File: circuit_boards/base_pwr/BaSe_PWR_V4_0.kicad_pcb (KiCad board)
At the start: 4 copper layers, 114.2 x 101.5 mm, 101 parts, among them J1 12VDC In, J10 Conn_01x04_Socket, J11 MOTOR, J12 USB3_A, J3 USB_B_Micro, J4 Conn_01x07_Pin, J5 Conn_02x06_Odd_Even, J6 USB3_B_Micro, J7 Conn_02x06_Odd_Even, J8 USB_C_Receptacle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

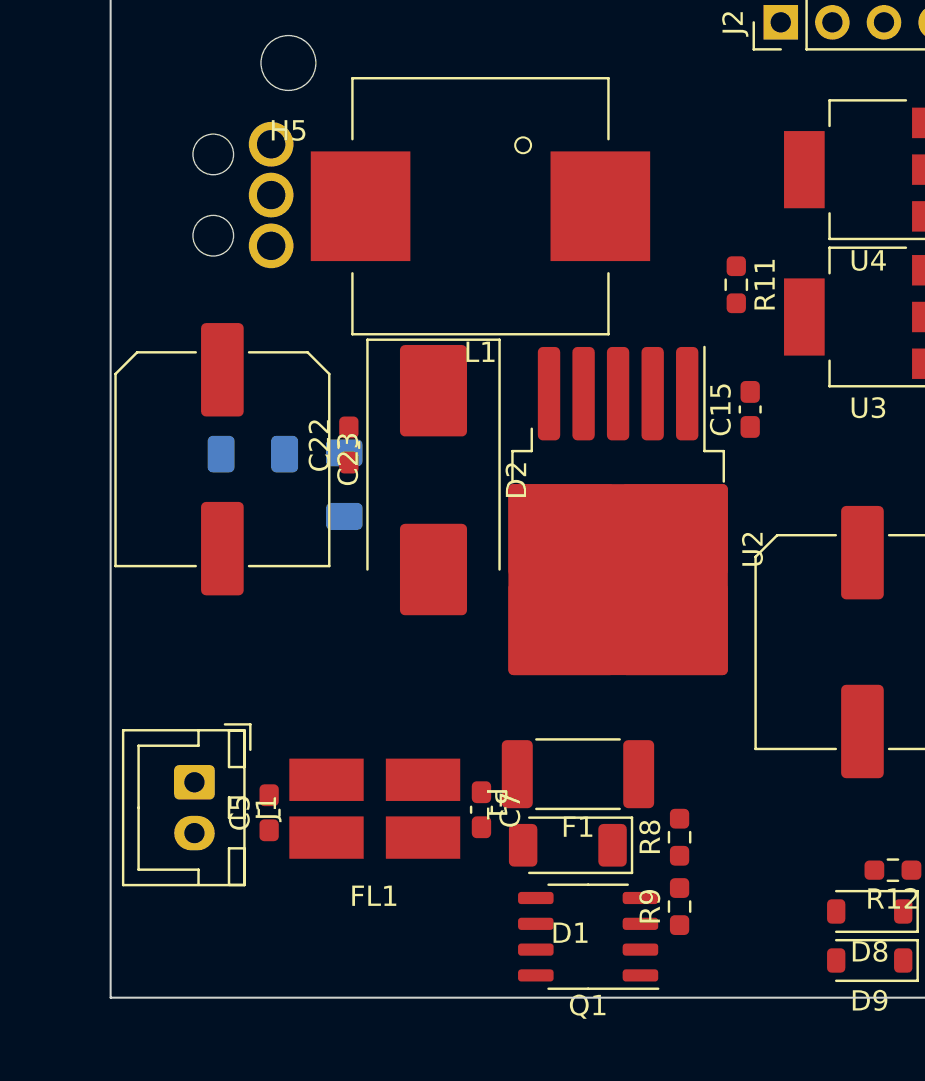
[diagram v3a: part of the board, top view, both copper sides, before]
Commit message: BaSe PWR V4.0: quasi final positioning before actual routing phase
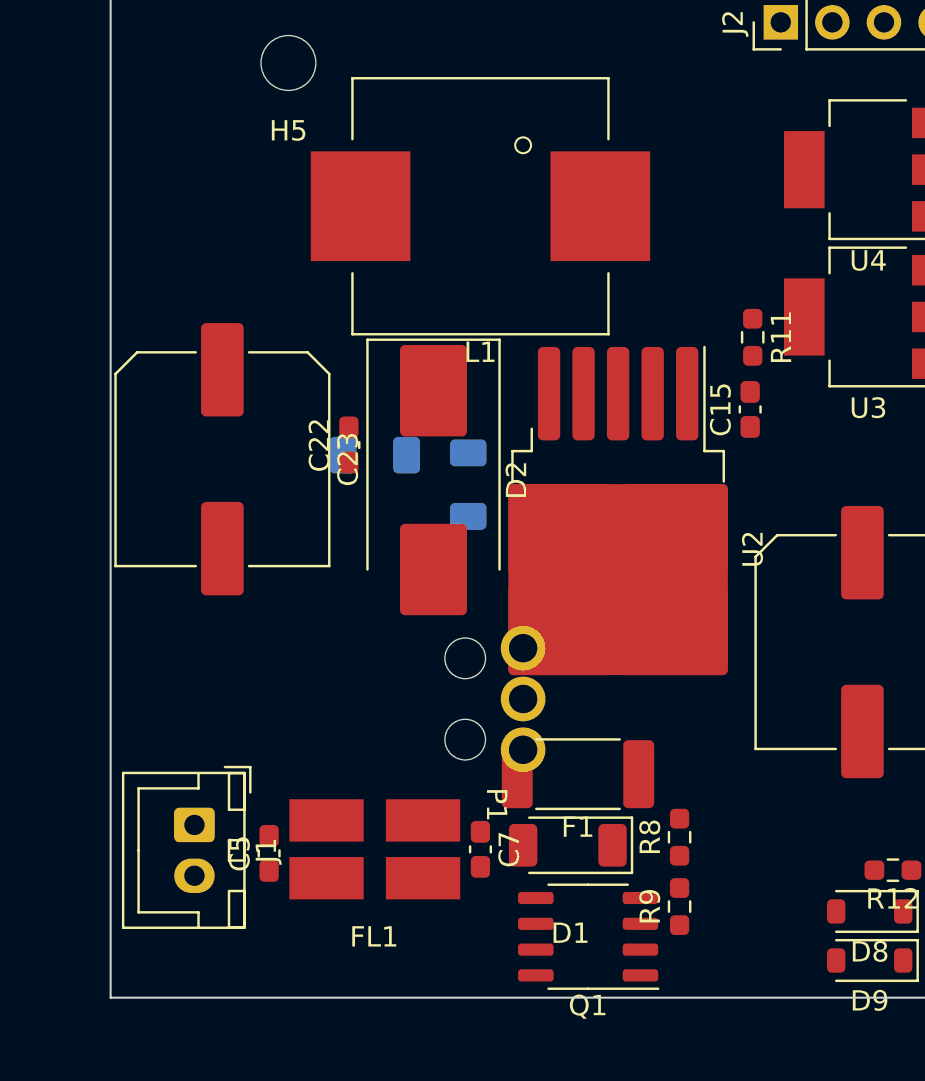
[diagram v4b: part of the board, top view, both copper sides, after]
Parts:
- moved U6 27.7 mm to (40.3, 98.8)
- moved C26 6.10 mm to (37.6, 88.2)
- moved FB1 6.00 mm to (33.0, 86.8)
- moved R11 2.71 mm to (51.6, 81.0)
- moved J1 2.10 mm to (24.1, 105.0)
- moved C5 2.00 mm to (27.8, 106.4)
- moved FL1 2.00 mm to (33.0, 106.2)
- moved C7 1.95 mm to (38.2, 106.2)
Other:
- board text added: "No Components here on BOTTOM"
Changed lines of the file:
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@@
   )
   (footprint "Capacitor_SMD:C_0603_1608Metric_Pad1.08x0.95mm_HandSolder" (layer "F.Cu")
-    (at 27.8 104.4 90)
+    (at 27.8 106.4 90)
     (descr "Capacitor SMD 0603 (1608 Metric), square (rectangular) end terminal, IPC_7351 nominal with elongated pad for handsoldering. (Body size source: IPC-SM-782 page 76, https://www.pcb-3d.com/wordpress/wp-content/uploads/ipc-sm-782a_amendment_1_and_2.pdf), generated with kicad-footprint-generator")
     (tags "capacitor handsolder")
@@
   )
   (footprint "Connector_JST:JST_XH_B2B-XH-A_1x02_P2.50mm_Vertical" (layer "F.Cu")
-    (at 24.125 102.9 -90)
+    (at 24.125 105 -90)
     (descr "JST XH series connector, B2B-XH-A (http://www.jst-mfg.com/product/pdf/eng/eXH.pdf), generated with kicad-footprint-generator")
     (tags "connector JST XH vertical")
@@
   )
   (footprint "Capacitor_SMD:C_0603_1608Metric_Pad1.08x0.95mm_HandSolder" (layer "F.Cu")
-    (at 38.25 104.25 -90)
+    (at 38.2 106.2 -90)
     (descr "Capacitor SMD 0603 (1608 Metric), square (rectangular) end terminal, IPC_7351 nominal with elongated pad for handsoldering. (Body size source: IPC-SM-782 page 76, https://www.pcb-3d.com/wordpress/wp-content/uploads/ipc-sm-782a_amendment_1_and_2.pdf), generated with kicad-footprint-generator")
     (tags "capacitor handsolder")
@@
   )
   (footprint "g7_emi:CMC_Laird_CM2021Y330R-10" (layer "F.Cu")
-    (at 33 104.2)
+    (at 33 106.2)
     (property "SPN" "240-2502-1-ND")
     (property "Sheetfile" "BaSe_PWR_V4_0.kicad_sch")
@@
   )
   (footprint "Resistor_SMD:R_0603_1608Metric_Pad0.98x0.95mm_HandSolder" (layer "F.Cu")
-    (at 50.79 78.4125 -90)
+    (at 51.6 81 -90)
     (descr "Resistor SMD 0603 (1608 Metric), square (rectangular) end terminal, IPC_7351 nominal with elongated pad for handsoldering. (Body size source: IPC-SM-782 page 72, https://www.pcb-3d.com/wordpress/wp-content/uploads/ipc-sm-782a_amendment_1_and_2.pdf), generated with kicad-footprint-generator")
     (tags "resistor handsolder")
@@
   )
   (footprint "Capacitor_SMD:C_1206_3216Metric_Pad1.33x1.80mm_HandSolder" (layer "B.Cu")
-    (at 31.5 88.25 90)
+    (at 37.6 88.25 90)
     (descr "Capacitor SMD 1206 (3216 Metric), square (rectangular) end terminal, IPC_7351 nominal with elongated pad for handsoldering. (Body size source: IPC-SM-782 page 76, https://www.pcb-3d.com/wordpress/wp-content/uploads/ipc-sm-782a_amendment_1_and_2.pdf), generated with kicad-footprint-generator")
     (tags "capacitor handsolder")
@@
     )
   )
-  (footprint "g7_switch:TS0101F020V4" (layer "B.Cu")
-    (at 27.9 74 -90)
+  (footprint "g7_switch:TS0101F020V4" locked (layer "B.Cu")
+    (at 40.3 98.8 -90)
     (property "Digikey" "EG4938-ND")
     (property "Sheetfile" "BaSe_PWR_V4_0.kicad_sch")
@@
     (fp_line (start 4.1 7.85) (end 4.1 1.25)
       (stroke (width 0.1) (type default)) (layer "B.Fab"))
-    (pad "" np_thru_hole circle (at -2 2.85 270) (size 2 2) (drill 2) (layers "F&B.Cu" "*.Mask"))
-    (pad "" np_thru_hole circle (at 2 2.85 270) (size 2 2) (drill 2) (layers "F&B.Cu" "*.Mask"))
-    (pad "C" thru_hole circle (at -2.5 0 270) (size 2.2 2.2) (drill 1.4) (layers "*.Cu" "*.Mask")
+    (pad "" np_thru_hole circle locked (at -2 2.85 270) (size 2 2) (drill 2) (layers "F&B.Cu" "*.Mask"))
+    (pad "" np_thru_hole circle locked (at 2 2.85 270) (size 2 2) (drill 2) (layers "F&B.Cu" "*.Mask"))
+    (pad "C" thru_hole circle locked (at -2.5 0 270) (size 2.2 2.2) (drill 1.4) (layers "*.Cu" "*.Mask")
       (net 1 "GND") (pinfunction "C") (pintype "bidirectional"))
-    (pad "NC" thru_hole circle (at 2.5 0 270) (size 2.2 2.2) (drill 1.4) (layers "*.Cu" "*.Mask")
+    (pad "NC" thru_hole circle locked (at 2.5 0 270) (size 2.2 2.2) (drill 1.4) (layers "*.Cu" "*.Mask")
       (net 119 "unconnected-(U6-PadNC)") (pinfunction "NC") (pintype "bidirectional+no_connect"))
-    (pad "NO" thru_hole circle (at 0 0 270) (size 2.2 2.2) (drill 1.4) (layers "*.Cu" "*.Mask")
+    (pad "NO" thru_hole circle locked (at 0 0 270) (size 2.2 2.2) (drill 1.4) (layers "*.Cu" "*.Mask")
       (net 118 "/~{endswitch_undocked}") (pinfunction "NO") (pintype "bidirectional"))
     (model ":G7_BAUTEILE:Diskrete Elektronik Bauteile/sw_ts0101f020v4/TS0101F020V4.step"
@@
   )
   (footprint "Capacitor_SMD:C_1206_3216Metric_Pad1.33x1.80mm_HandSolder" (layer "B.Cu")
-    (at 27 86.75)
+    (at 33 86.8)
     (descr "Capacitor SMD 1206 (3216 Metric), square (rectangular) end terminal, IPC_7351 nominal with elongated pad for handsoldering. (Body size source: IPC-SM-782 page 76, https://www.pcb-3d.com/wordpress/wp-content/uploads/ipc-sm-782a_amendment_1_and_2.pdf), generated with kicad-footprint-generator")
     (tags "capacitor handsolder")
@@
     (effects (font (size 1.5 1.5) (thickness 0.1)) (justify left top))
   )
+  (gr_text "No Components\nhere on BOTTOM" (at 29.6 94.6 90) (layer "Cmts.User")
+    (effects (font (size 1 1) (thickness 0.15)) (justify left bottom))
+  )
   (dimension (type aligned) (layer "Dwgs.User")
     (pts (xy 19.5 126) (xy 29.5 126))
@@
   (segment (start 88.012501 153.675) (end 88.172501 153.835) (width 0.18) (layer "B.Cu") (net 17))
   (segment (start 93.931654 134.835) (end 94.914999 134.835) (width 0.18) (layer "B.Cu") (net 17))
+  (zone (net 0) (net_name "") (layer "Cmts.User") (hatch edge 0.5)
+    (connect_pads (clearance 0))
+    (min_thickness 0.25) (filled_areas_thickness no)
+    (keepout (tracks allowed) (vias allowed) (pads allowed) (copperpour allowed) (footprints not_allowed))
+    (fill (thermal_gap 0.5) (thermal_bridge_width 0.5))
+    (polygon
+      (pts
+        (xy 20 63.6)
+        (xy 31 63.6)
+        (xy 31 113.4)
+        (xy 20 113.4)
+      )
+    )
+  )
   (group "group-boardStackUp" (id 18bffec4-4616-426a-9e8f-255a5ab01ded)
     (members

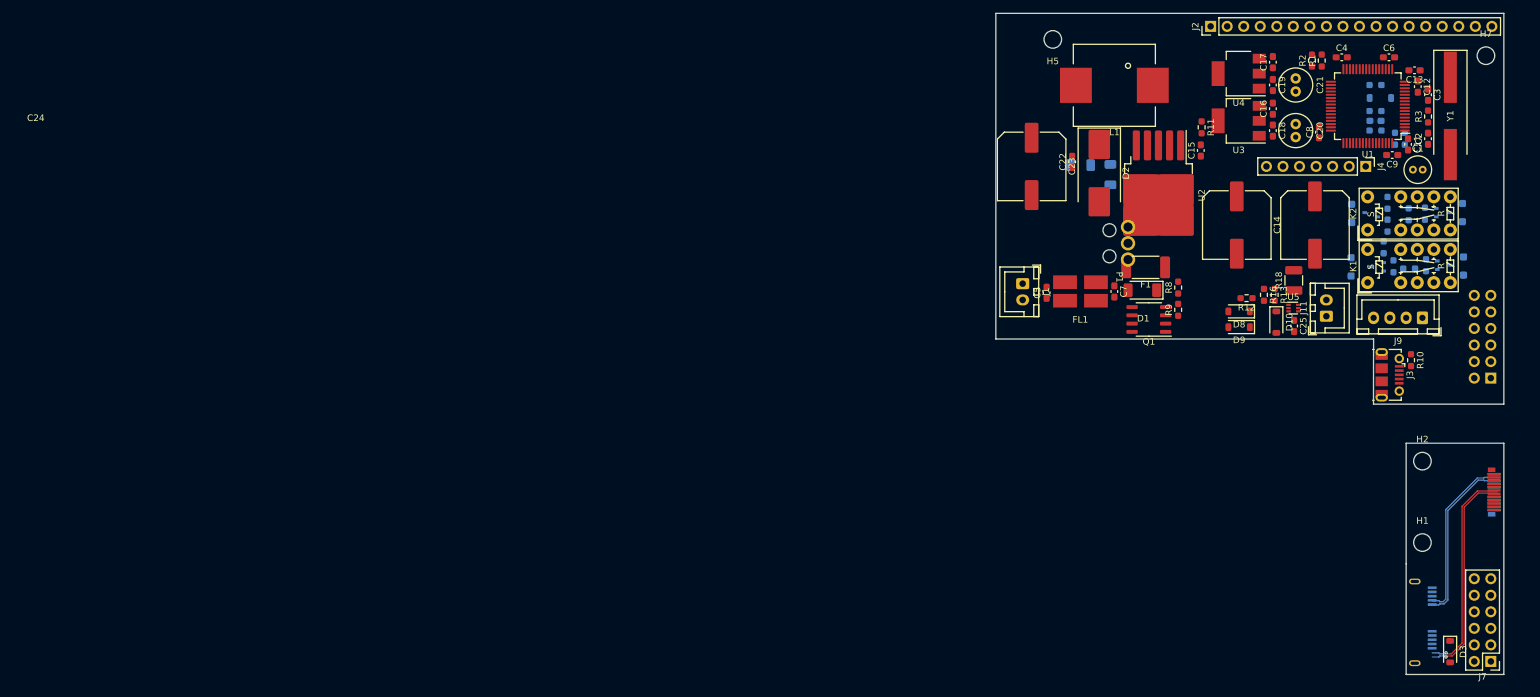
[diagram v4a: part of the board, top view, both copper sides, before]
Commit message: BaSe PWR V4.0: probably final placement, start routing
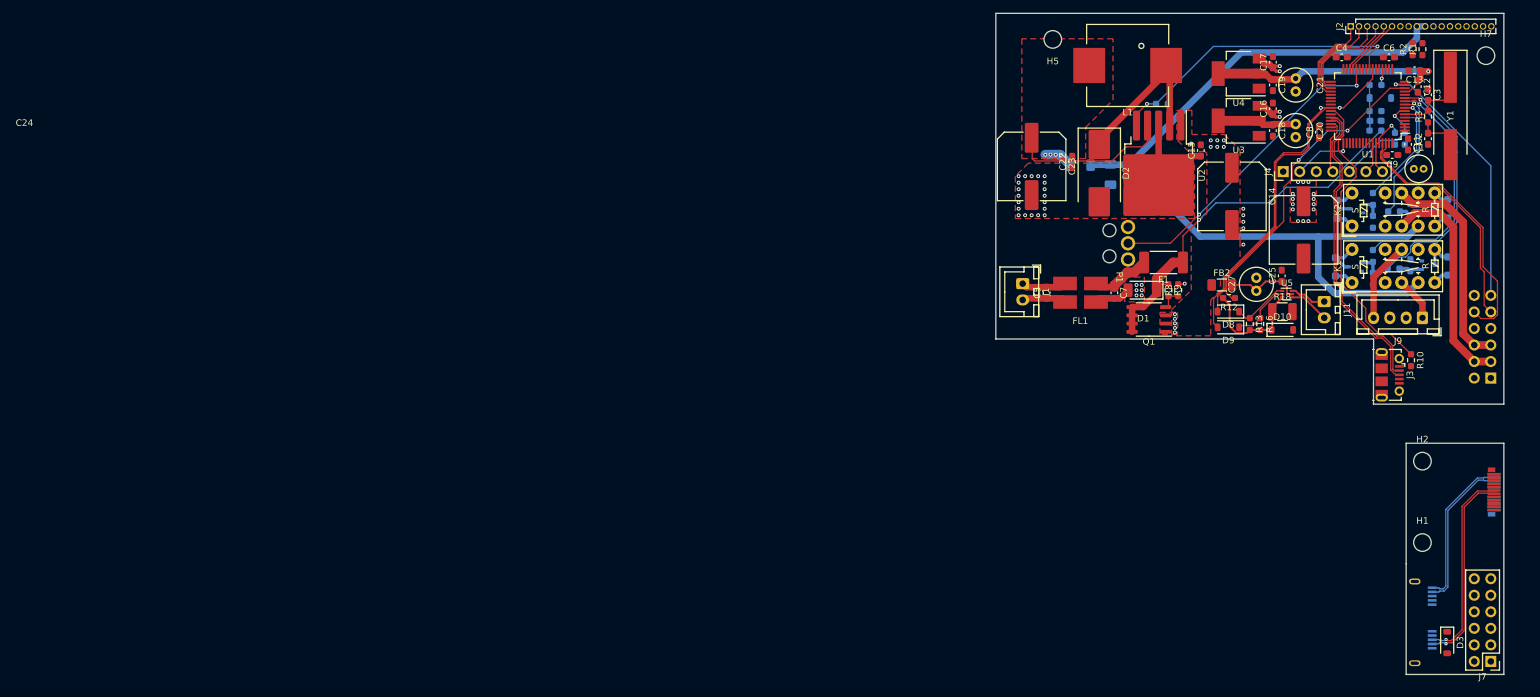
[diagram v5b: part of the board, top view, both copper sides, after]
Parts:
- added C27: 22µF, Capacitor_THT:C_Radial_D5.0mm_H11.0mm_P2.00mm, F.Cu at (60.0, 106.1)
- added FB2: FerriteBead, Capacitor_SMD:C_1206_3216Metric_Pad1.33x1.80mm_HandSolder, F.Cu at (54.7, 105.2)
- J2: footprint Connector_PinHeader_2.54mm:PinHeader_1x18_P2.54mm_Vertical -> Connector_PinHeader_1.27mm:PinHeader_1x18_P1.27mm_Vertical
- R11: moved to B.Cu
- moved J2 21.5 mm to (74.5, 65.5)
- moved R1 15.6 mm to (85.5, 69.0)
- moved R2 15.6 mm to (84.0, 69.0)
- moved J4 12.7 mm to (64.1, 87.8), turned to 90 degrees
- moved C25 7.93 mm to (63.9, 103.8), turned to 90 degrees
- moved R11 7.07 mm to (45.5, 77.4), turned to 0 degrees
- moved R13 5.89 mm to (59.0, 111.2)
- moved R18 5.11 mm to (64.0, 109.3), turned to 0 degrees
- moved R16 4.52 mm to (60.6, 111.2)
- moved C14 4.46 mm to (56.2, 91.6)
- moved 2k3 3.68 mm to (77.9, 104.2)
- moved L1 3.67 mm to (40.2, 71.5)
- moved Q2 3.40 mm to (75.2, 102.4)
- moved R9 3.37 mm to (46.5, 106.0), turned to -90 degrees
- moved U2 3.05 mm to (45.0, 88.4)
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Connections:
- C25 pad 1: +12V -> /12v_motor
- J11 pad 1: Net-(J11-Pin_1) -> /motor1
- J11 pad 2: Net-(J11-Pin_2) -> /motor2
- J4 pad 3: GND1 -> GND
- J7 pad 11: /stator_supply_sense -> /stator_supply_sense_
- P1 pad A5: /stator_supply_sense -> /stator_supply_sense_
- U5 pad 4: Net-(J11-Pin_1) -> /motor2
- U5 pad 5: +12V -> /12v_motor
- U5 pad 6: Net-(J11-Pin_2) -> /motor1
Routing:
- net +5V: track 0.00 -> 134.2 mm
- net /12V_nProt: track 0.00 -> 59.9 mm, vias 0 -> 1
- net /in2_mcu: track 0.00 -> 53.6 mm, vias 0 -> 2
- net /~{endswitch_undocked}: track 0.00 -> 48.1 mm, vias 0 -> 2
- net /imotor_prot: track 0.00 -> 47.5 mm, vias 0 -> 2
- net /~{LM2596S_ON}: track 0.00 -> 47.0 mm, vias 0 -> 2
- net /USB_D+: track 0.00 -> 46.6 mm
- net /USB_D-: track 0.00 -> 46.5 mm
- net /vbus_sense: track 0.00 -> 46.4 mm
- net /stator_supply_sense: track 0.00 -> 41.1 mm, vias 0 -> 1
- net /i2c1_sda: track 0.00 -> 41.0 mm
- net /in1_mcu: track 0.00 -> 40.6 mm
- net +3.3VA: track 0.00 -> 39.1 mm, vias 0 -> 1
- net /sw_sbu_off: track 0.00 -> 38.1 mm, vias 0 -> 1
- net /sw_sbu_on: track 0.00 -> 37.1 mm, vias 0 -> 1
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- added copper zone on F.Cu, net +12V
- added copper zone on In2.Cu, net +12V
- added copper zone on In2.Cu, net +3V3_STBY
- added copper zone on F.Cu, net /+5v_out
- added copper zone on F.Cu, net GND
- added copper zone on In1.Cu, net GND

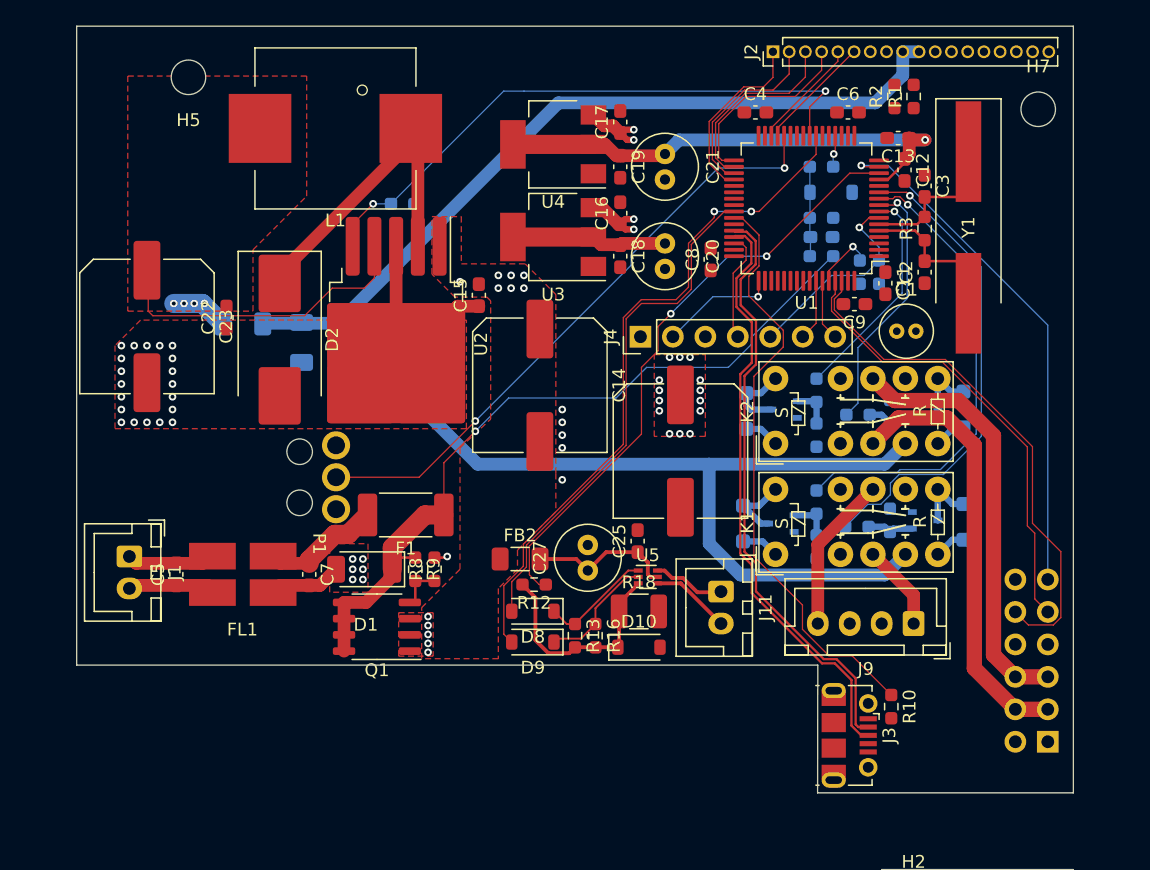
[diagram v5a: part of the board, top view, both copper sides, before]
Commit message: BaSe_PWR_V4_0: add gnd planes on outer layers, thicked up DC input tracks to carry 5A
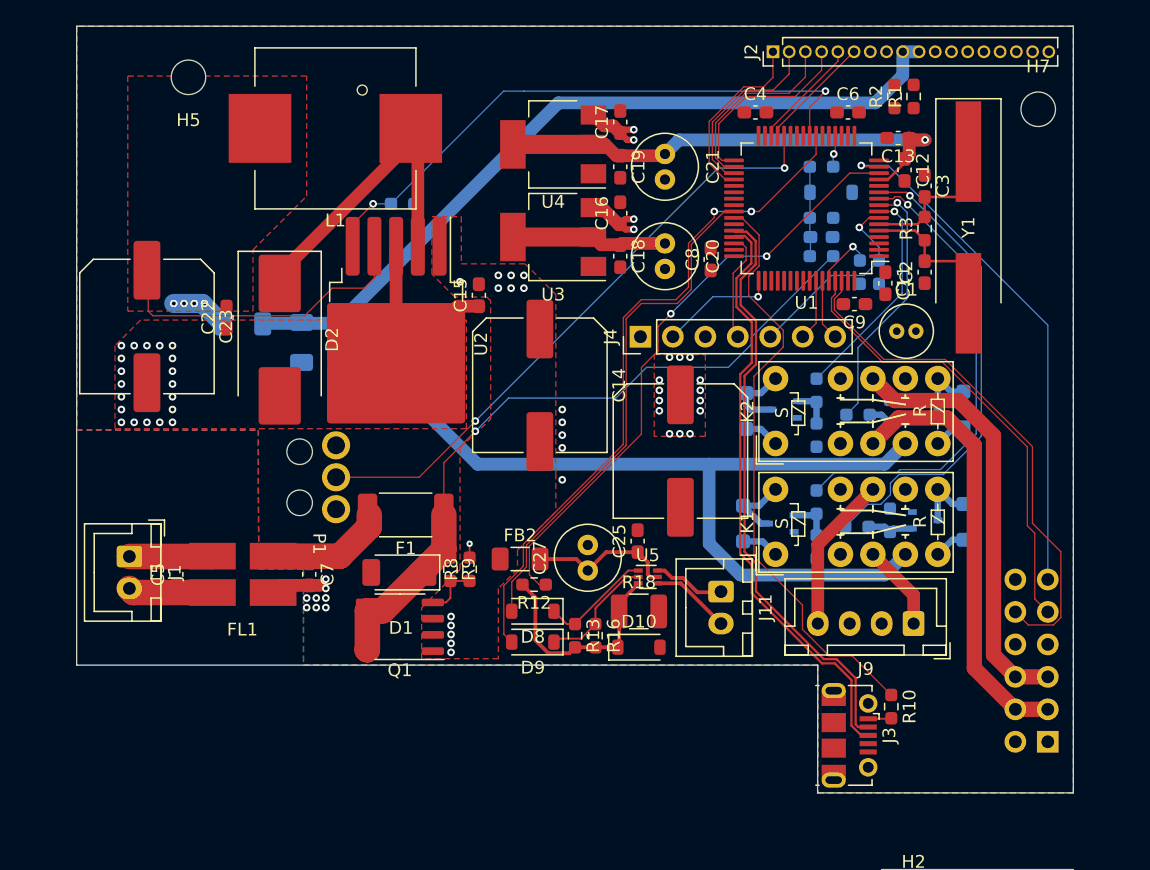
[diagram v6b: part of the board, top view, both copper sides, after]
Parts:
- moved D1 2.76 mm to (45.2, 106.2)
- moved R8 2.75 mm to (50.8, 106.0)
- moved R9 2.75 mm to (49.2, 106.0)
- moved Q1 1.80 mm to (45.3, 110.5)
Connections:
- net /12V_nProt renamed /DC_preprot
- net Net-(C7-Pad1) renamed /DC_prefuse
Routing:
- net /DC_preprot: track 59.9 -> 55.3 mm
- net Net-(J3-VBUS): track 0.00 -> 1.82 mm
- net GND: track 20.4 -> 18.7 mm, vias 32 -> 34
- net Net-(Q1-G): track 3.61 -> 4.36 mm
- net /DC_IN+: track 7.04 -> 6.51 mm
- added copper zone on B.Cu, net GND
